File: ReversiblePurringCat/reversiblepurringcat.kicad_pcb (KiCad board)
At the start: 2 copper layers, 230.3 x 90.7 mm, 78 parts, among them J1 ScreenL, J2 ScreenR, SW0 SW_Push, SW1 SW_Push, SW10 SW_Push, SW11 SW_Push, SW12 SW_Push, SW13 SW_Push, SW14 SW_Push, SW15 SW_Push, SW16 SW_Push, SW17 SW_Push, SW18 SW_Push, SW19 SW_Push, SW2 SW_Push, SW20 SW_Push, SW21 SW_Push, SW22 SW_Push, SW23 SW_Push, SW24 SW_Push, SW25 SW_Push, SW26 SW_Push, SW27 SW_Push, SW28 SW_Push, SW29 SW_Push, SW3 SW_Push, SW30 SW_Push, SW31 SW_Push, SW4 SW_Push, SW5 SW_Push, SW6 SW_Push, SW7 SW_Push, SW8 SW_Push, SW9 SW_Push, U1 ProMicro-kbd, U2 ProMicro-kbd

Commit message: reversible updates
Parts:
- removed Bat+r1, BatGND4: MountingHole_Pad, kbd:1pin_conn
- removed D15, D16, D17, D18, D19, D23, D24, D25, D29, D30, D31, D4, D5, D6, D7, D8, D9: D, kbd:D3_SMD_v2
- removed J2: ScreenR, Connector_PinHeader_2.54mm:PinHeader_1x05_P2.54mm_Vertical
- removed RSW2: SW_Push, Button_Switch_SMD:SW_SPST_CK_RS282G05A3
- removed SW15, SW16, SW17, SW18, SW19, SW23, SW24, SW25, SW29, SW30, SW31, SW5, SW6, SW7, SW8, SW9: SW_Push, keyswitches:Kailh_socket_PG1350
- removed SW_POWER2: SW_SPDT, Button_Switch_SMD:SW_SPDT_PCM12
- removed U2: ProMicro-kbd, kbd:ProMicro_v3
- removed mouse-bite-2mm-slot (x2): VAL**, Duckyb-Parts:mouse-bite-5mm-slot-with-space-for-track
- SW0, SW1, SW10, SW11, SW12, SW13, SW14, SW2, SW20, SW21, SW22, SW26, SW27, SW28, SW3, SW4: footprint keyswitches:Kailh_socket_PG1350 -> keyswitches:Kailh_socket_PG1350_reversible
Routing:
- net row_0: track 175.1 -> 0.00 mm
- net row_1: track 155.3 -> 0.00 mm
- net col2r: track 151.5 -> 0.00 mm, vias 3 -> 0
- net col1r: track 141.6 -> 0.00 mm, vias 1 -> 0
- net col3r: track 139.6 -> 0.00 mm, vias 4 -> 0
- net col4r: track 133.1 -> 0.00 mm, vias 4 -> 0
- net col3: track 131.5 -> 2.43 mm, vias 5 -> 1
- net row_0r: track 128.1 -> 0.00 mm
- net col1: track 121.2 -> 0.23 mm, vias 3 -> 0
- net row_2: track 119.5 -> 0.00 mm
- net col2: track 116.9 -> 0.31 mm, vias 4 -> 0
- net row_1r: track 114.1 -> 0.00 mm
- net col5r: track 106.1 -> 0.00 mm, vias 4 -> 0
- net col4: track 107.5 -> 2.85 mm, vias 5 -> 1
- net col5: track 85.4 -> 0.73 mm, vias 3 -> 0
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- removed copper zone on B.Cu, net gnd
- removed copper zone on F.Cu, net gnd
- removed copper zone on B.Cu, net gnd_r
- removed copper zone on F.Cu, net gnd_r
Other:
- board size 230.3 x 90.7 mm -> 114 x 90.7 mm
- board text removed: "15/B1"

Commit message: working on diodeless
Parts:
- removed SW26: SW_Push, keyswitches:Kailh_socket_PG1350_reversible
- added D4: D, kbd:D3_SMD_v2, B.Cu at (216.5, 35.8)
- U1: value ProMicro-kbd -> nice!nano v2; footprint kbd:ProMicro_v3 -> nice-nano-kicad:nice_nano
- moved D26 0.22 mm to (197.2, 81.8)
- moved D27 0.08 mm to (218.6, 84.9)
- moved D3 0.07 mm to (198.5, 27.7)
- turned RSW1 to 145 degrees
- turned U1 to -90 degrees
- renumbered SW0 to 0/9, SW1 to 1/8, SW10 to 10/19, SW11 to 11/18, SW12 to 12/17, SW2 to 2/7, SW3 to 3/6, SW4 to 4/5
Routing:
- net gnd: track 0.00 -> 8.95 mm, vias 0 -> 1
- net reset: track 0.00 -> 8.75 mm, vias 0 -> 1

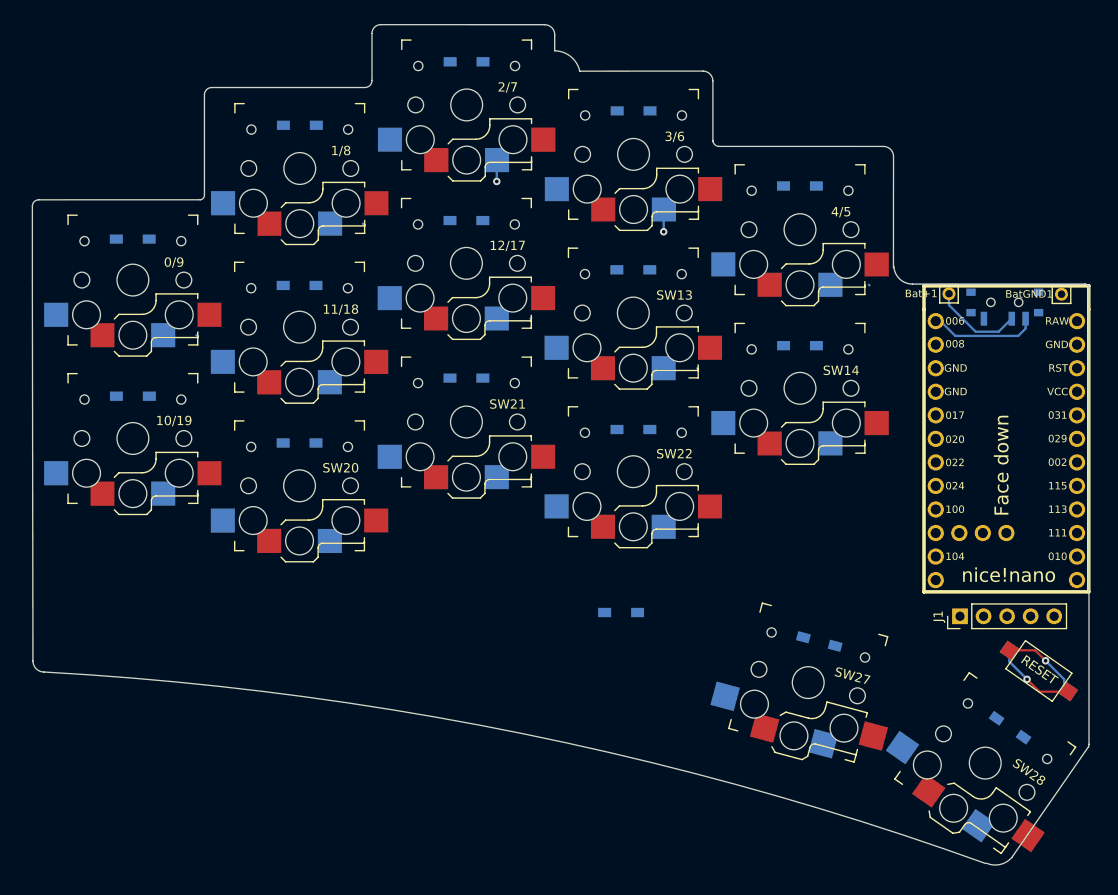
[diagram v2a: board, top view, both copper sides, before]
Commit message: moving back to reversible. still diodeless. needs case mounts
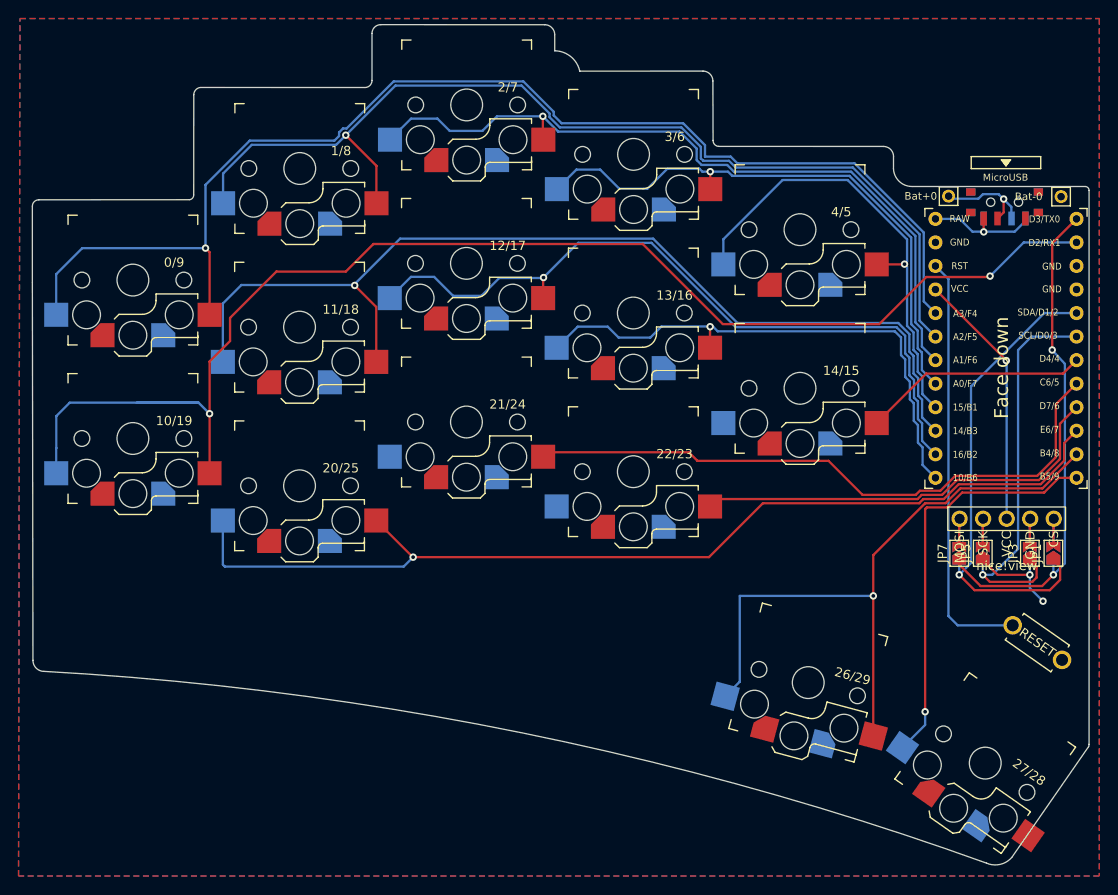
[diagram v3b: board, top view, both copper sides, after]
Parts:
- removed D0, D1, D10, D11, D12, D13, D14, D2, D20, D21, D22, D26, D27, D28, D3, D4: D, kbd:D3_SMD_v2
- removed J1: ScreenL, Connector_PinHeader_2.54mm:PinHeader_1x05_P2.54mm_Vertical
- removed RSW1: SW_Push, Button_Switch_SMD:SW_SPST_CK_RS282G05A3
- added J0: nice!view, nice_view:nice_view, F.Cu at (238.8, 55.2)
- added JP0: Jumper_2_Small_Open, Jumper:SolderJumper-2_P1.3mm_Open_TrianglePad1.0x1.5mm, B.Cu at (233.7, 75.4)
- added JP1: Jumper_2_Small_Open, Jumper:SolderJumper-2_P1.3mm_Open_TrianglePad1.0x1.5mm, F.Cu at (243.8, 75.4)
- added JP2: Jumper_2_Small_Open, Jumper:SolderJumper-2_P1.3mm_Open_TrianglePad1.0x1.5mm, B.Cu at (236.2, 75.4)
- added JP3: Jumper_2_Small_Open, Jumper:SolderJumper-2_P1.3mm_Open_TrianglePad1.0x1.5mm, F.Cu at (241.3, 75.4)
- added JP4: Jumper_2_Small_Open, Jumper:SolderJumper-2_P1.3mm_Open_TrianglePad1.0x1.5mm, B.Cu at (241.3, 75.4)
- added JP5: Jumper_2_Small_Open, Jumper:SolderJumper-2_P1.3mm_Open_TrianglePad1.0x1.5mm, F.Cu at (236.2, 75.4)
- added JP6: Jumper_2_Small_Open, Jumper:SolderJumper-2_P1.3mm_Open_TrianglePad1.0x1.5mm, B.Cu at (243.8, 75.4)
- added JP7: Jumper_2_Small_Open, Jumper:SolderJumper-2_P1.3mm_Open_TrianglePad1.0x1.5mm, F.Cu at (233.7, 75.4)
- added RSW0: SW_Push, kbd:ResetSW, F.Cu at (242.1, 85.0)
- 0/9, 1/8, 10/19, 11/18, 12/17, 2/7, 3/6, 4/5: footprint keyswitches:Kailh_socket_PG1350_reversible -> chelming-kbd:choc_v1_hotswap_reversible_no_extras
- 13/16: renamed from SW13; footprint keyswitches:Kailh_socket_PG1350_reversible -> chelming-kbd:choc_v1_hotswap_reversible_no_extras
- 14/15: renamed from SW14; footprint keyswitches:Kailh_socket_PG1350_reversible -> chelming-kbd:choc_v1_hotswap_reversible_no_extras
- 20/25: renamed from SW20; footprint keyswitches:Kailh_socket_PG1350_reversible -> chelming-kbd:choc_v1_hotswap_reversible_no_extras
- 21/24: renamed from SW21; footprint keyswitches:Kailh_socket_PG1350_reversible -> chelming-kbd:choc_v1_hotswap_reversible_no_extras
- 22/23: renamed from SW22; footprint keyswitches:Kailh_socket_PG1350_reversible -> chelming-kbd:choc_v1_hotswap_reversible_no_extras
- 26/29: renamed from SW27; footprint keyswitches:Kailh_socket_PG1350_reversible -> chelming-kbd:choc_v1_hotswap_reversible_no_extras
- 27/28: renamed from SW28; footprint keyswitches:Kailh_socket_PG1350_reversible -> chelming-kbd:choc_v1_hotswap_reversible_no_extras
- SW_PWR0: renamed from SW_POWER1; footprint Button_Switch_SMD:SW_SPDT_PCM12 -> chelming-kbd:SW_SPDT_PCM12_REVERSIBLE
- U0: renamed from U1; value nice!nano v2 -> ProMicro-kbd; footprint nice-nano-kicad:nice_nano -> kbd:ProMicro_v3
- moved SW_PWR0 10.8 mm to (238.6, 37.8)
- moved Bat-0 10.5 mm to (244.7, 36.9)
- moved U0 10.5 mm to (238.7, 53.8), turned to 0 degrees
- moved Bat+0 10.5 mm to (232.5, 36.9)
- renumbered Bat+1 to Bat+0, BatGND1 to Bat-0
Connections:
- 0/9 pad 1: col1 -> gnd
- 0/9 pad 2: Net-(D0-A) -> s0
- 1/8 pad 1: col2 -> gnd
- 1/8 pad 2: Net-(D1-A) -> s1
- 10/19 pad 1: col1 -> gnd
- 10/19 pad 2: Net-(D10-A) -> s10
- 11/18 pad 1: col2 -> gnd
- 11/18 pad 2: Net-(D11-A) -> s11
- 12/17 pad 1: col3 -> gnd
- 12/17 pad 2: Net-(D12-A) -> s12
- 13/16 pad 1: col4 -> gnd
- 13/16 pad 2: Net-(D13-A) -> s13
- 14/15 pad 1: col5 -> gnd
- 14/15 pad 2: Net-(D14-A) -> s14
- 2/7 pad 1: col3 -> gnd
- 2/7 pad 2: Net-(D2-A) -> s2
- 20/25 pad 1: col2 -> gnd
- 20/25 pad 2: Net-(D20-A) -> s20
- 21/24 pad 1: col3 -> gnd
- 21/24 pad 2: Net-(D21-A) -> s21
- 22/23 pad 1: col4 -> gnd
- 22/23 pad 2: Net-(D22-A) -> s22
- 26/29 pad 1: col4 -> gnd
- 26/29 pad 2: Net-(D27-A) -> s26
- 27/28 pad 1: col5 -> gnd
- 27/28 pad 2: Net-(D28-A) -> s27
- 3/6 pad 1: col4 -> gnd
- 3/6 pad 2: Net-(D3-A) -> s3
- 4/5 pad 1: col5 -> gnd
- 4/5 pad 2: Net-(D4-A) -> s4
- U0 pad 10: row_3 -> s20
- U0 pad 11: unconnected-(U1-P1.04-Pad11) -> s26
- U0 pad 12: unconnected-(U1-P1.06-Pad12) -> s27
- U0 pad 13: unconnected-(U1-NFC1/P0.09-Pad13) -> s13
- U0 pad 14: unconnected-(U1-NFC2/P0.10-Pad14) -> s12
- U0 pad 15: col5 -> s11
- U0 pad 16: col4 -> s4
- U0 pad 17: col3 -> s3
- U0 pad 18: col2 -> s2
- U0 pad 19: col1 -> s1
- U0 pad 2: unconnected-(U1-RX1/P0.08-Pad2) -> s10
- U0 pad 20: col0 -> s0
- U0 pad 7: row_0 -> s14
- U0 pad 8: row_1 -> s21
- U0 pad 9: row_2 -> s22
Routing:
- net s10: track 0.00 -> 150.0 mm, vias 0 -> 2
- net s0: track 0.00 -> 135.1 mm, vias 0 -> 1
- net s1: track 0.00 -> 110.4 mm, vias 0 -> 1
- net s20: track 0.00 -> 109.8 mm, vias 0 -> 1
- net s11: track 0.00 -> 108.6 mm, vias 0 -> 1
- net s2: track 0.00 -> 81.8 mm, vias 0 -> 1
- net s12: track 0.00 -> 80.3 mm, vias 0 -> 1
- net s26: track 0.00 -> 71.9 mm, vias 0 -> 1
- net s21: track 0.00 -> 68.0 mm
- net s3: track 0.00 -> 62.7 mm, vias 0 -> 1
- net s13: track 0.00 -> 58.5 mm, vias 0 -> 1
- net CS: track 0.00 -> 54.4 mm, vias 0 -> 2
- net MOSI: track 0.00 -> 51.6 mm, vias 0 -> 1
- net s4: track 0.00 -> 50.5 mm, vias 0 -> 1
- net s22: track 0.00 -> 46.2 mm
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- added copper zone on B.Cu, net gnd
- added copper zone on F.Cu, net gnd
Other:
- outline, holes or cut-outs redrawn
- board text removed: "RESET"

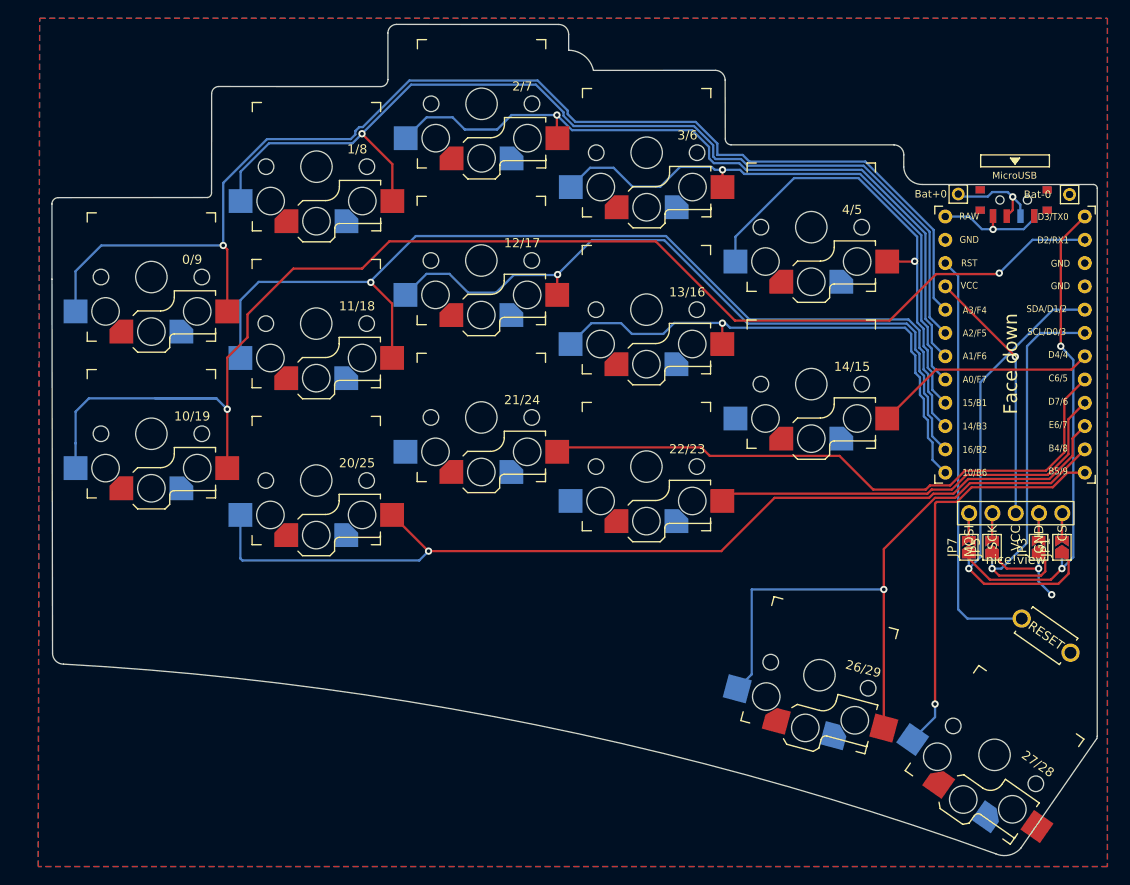
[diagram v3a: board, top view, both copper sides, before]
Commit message: added mounting holes
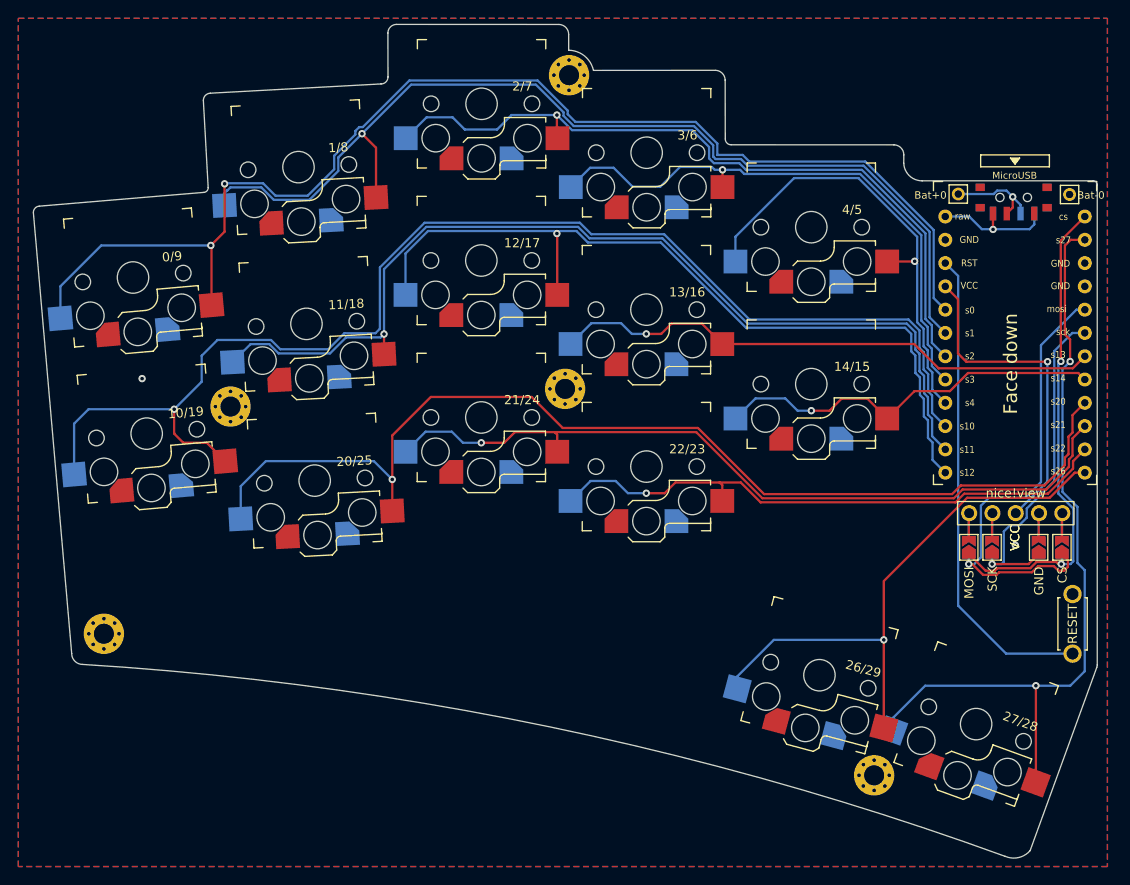
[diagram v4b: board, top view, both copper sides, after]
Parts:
- added H0: MountingHole_Pad, MountingHole:MountingHole_2.2mm_M2_Pad_Via, F.Cu at (190.1, 23.9)
- added H1: MountingHole_Pad, MountingHole:MountingHole_2.2mm_M2_Pad_Via, F.Cu at (189.6, 58.1)
- added H2: MountingHole_Pad, MountingHole:MountingHole_2.2mm_M2_Pad_Via, F.Cu at (223.4, 100.3)
- added H3: MountingHole_Pad, MountingHole:MountingHole_2.2mm_M2_Pad_Via, F.Cu at (153.1, 60.1)
- added H4: MountingHole_Pad, MountingHole:MountingHole_2.2mm_M2_Pad_Via, F.Cu at (139.3, 84.8)
- Bat+0, Bat-0: footprint kbd:1pin_conn -> keyboard:1pin_conn
- U0: footprint kbd:ProMicro_v3 -> keyboard:ProMicro_v3
- moved 27/28 3.91 mm to (234.5, 94.7), turned to -20 degrees
- moved RSW0 3.16 mm to (245.0, 83.8), turned to 90 degrees
- moved 0/9 2.00 mm to (142.5, 46.0), turned to 5 degrees
- moved 1/8 1.96 mm to (160.6, 33.9), turned to 3 degrees
- moved 11/18 1.07 mm to (161.4, 51.0), turned to 3 degrees
- moved 10/19 0.51 mm to (144.0, 63.0), turned to 5 degrees
- moved SW_PWR0 0.27 mm to (238.6, 37.6)
- moved 20/25 0.17 mm to (162.3, 68.1), turned to 3 degrees
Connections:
- U0 pad 10: s20 -> s21
- U0 pad 11: s26 -> s22
- U0 pad 12: s27 -> s26
- U0 pad 13: s13 -> s12
- U0 pad 14: s12 -> s11
- U0 pad 15: s11 -> s10
- U0 pad 2: s10 -> s27
- U0 pad 7: s14 -> s13
- U0 pad 8: s21 -> s14
- U0 pad 9: s22 -> s20
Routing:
- net s27: track 44.5 -> 85.4 mm, vias 1 -> 2
- net s14: track 24.4 -> 43.4 mm, vias 0 -> 1
- net s21: track 68.0 -> 86.1 mm, vias 0 -> 1
- net s22: track 46.2 -> 63.9 mm, vias 0 -> 1
- net s10: track 150.0 -> 139.2 mm, vias 2 -> 1
- net gnd: track 10.8 -> 0.00 mm
- net s26: track 71.9 -> 61.8 mm
- net s20: track 109.8 -> 119.2 mm
- net s12: track 80.3 -> 89.0 mm
- net vcc: track 27.9 -> 36.0 mm
- net reset: track 45.7 -> 52.6 mm
- net SCK: track 43.4 -> 38.0 mm
- net s13: track 58.5 -> 60.8 mm
- net s0: track 135.1 -> 137.1 mm, vias 1 -> 2
- net s11: track 108.6 -> 106.7 mm
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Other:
- board size 114 x 90.7 mm -> 116 x 90.9 mm
- board text added: "Face up"
- board text added: "VCC"
- board text added: "s14"
